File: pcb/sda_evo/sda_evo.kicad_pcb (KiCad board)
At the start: 4 copper layers, 61.5 x 105.9 mm, 156 parts, among them J1 PROG, J10 SPKR, J11 AudioJack, J2 USB_C_Receptacle_USB2.0, J3 LCD_CONN, J4 INT_EXP, J5 BATT, J9 Micro_SD_Card_Det, Q1 IRLML6302, SW1 RESET, SW2 BTN_A, SW3 BTN_B, SW4 BTN_UP, SW5 BTN_DOWN, SW6 BTN_LEFT, SW7 BTN_RIGHT, SW8 BTN_PWR, U1 USBLC6, U10 STM32H743ZITx, U11 USBLC6, U12 AP22802AW5-7, U13 LM4861, U2 TLV431, U3 USBLC6, U4 AP22802AW5-7, U5 FT230XS, U6 MCP73831-2-OT, U7 PCM5102, U8 NCP1529, U9 LMR62014XMF, Y1 16Mhz, Y2 32.768

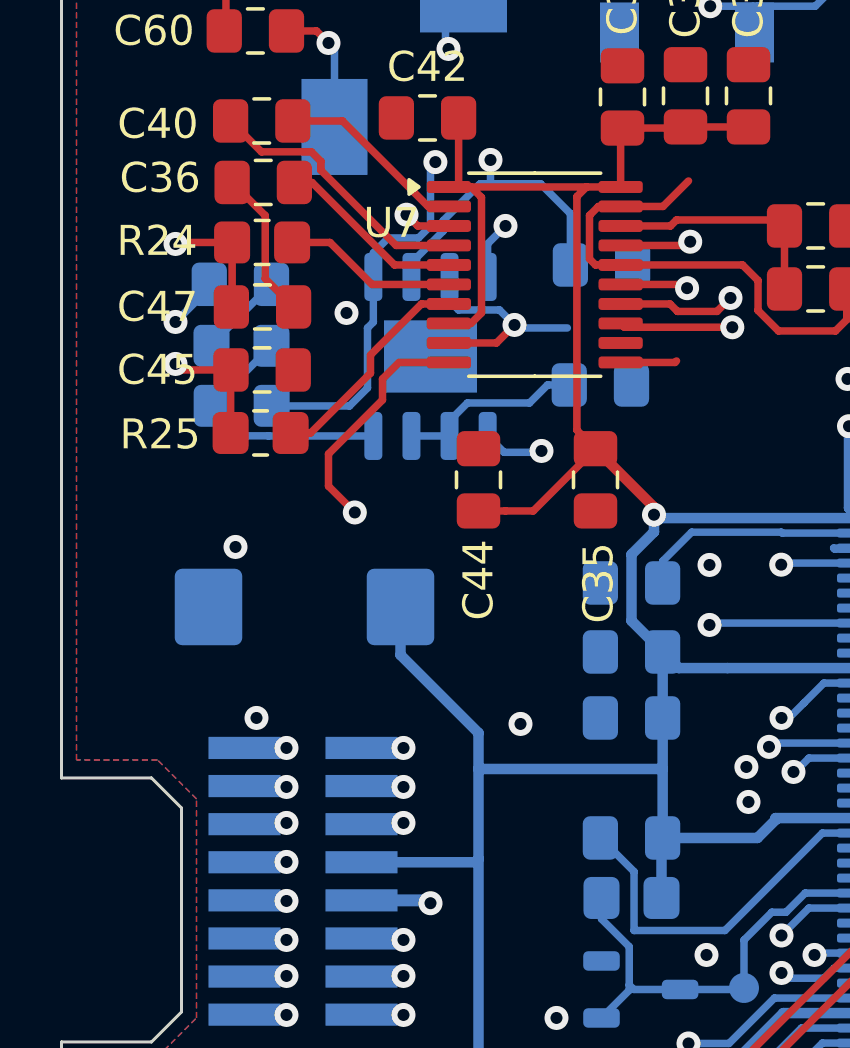
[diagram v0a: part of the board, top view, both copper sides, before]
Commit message: cap moved out of te way
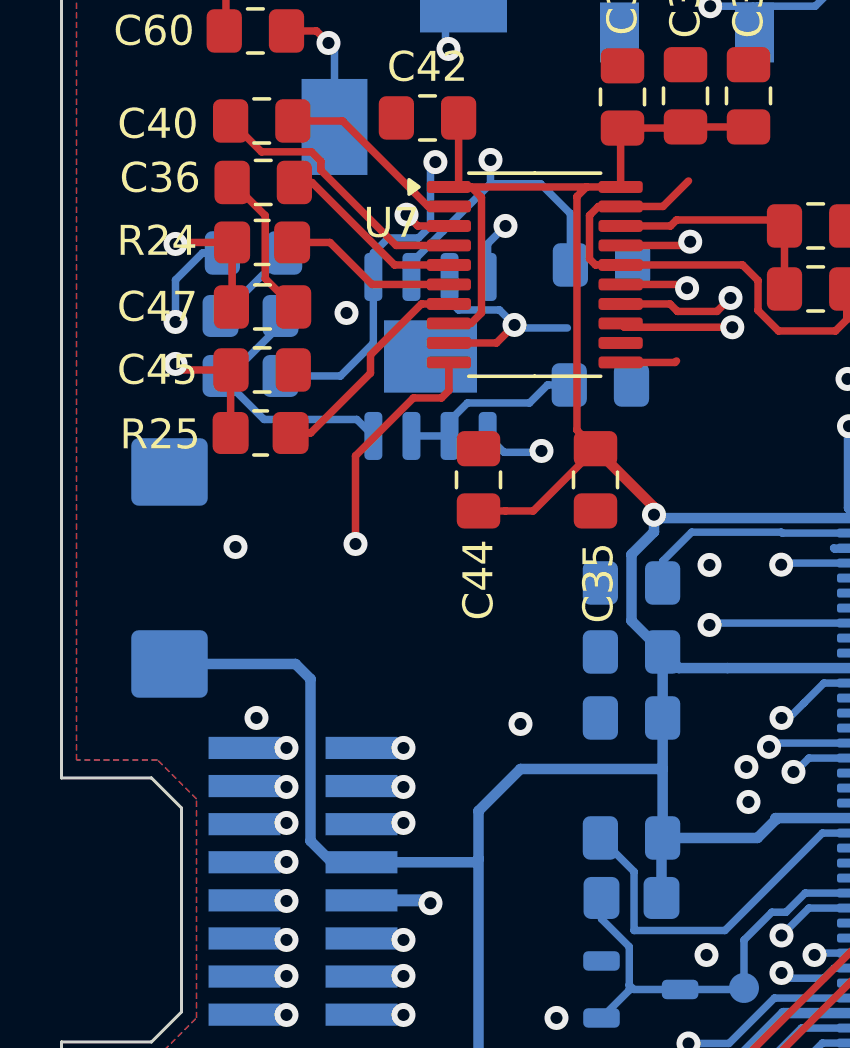
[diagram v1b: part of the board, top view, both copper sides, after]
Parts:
- moved C20 4.68 mm to (62.1, 80.0), turned to 90 degrees
- moved C58 1.13 mm to (64.9, 69.5)
- moved R35 1.04 mm to (64.8, 71.6)
- moved R31 1.04 mm to (64.8, 73.6)
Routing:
- net +3V3: track 478.2 -> 483.6 mm
- net BEEPER: track 39.2 -> 40.8 mm
- net Net-(C58-Pad2): track 2.99 -> 4.16 mm
- net Net-(J10-Pin_2): track 22.2 -> 21.3 mm

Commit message: datasheets cleanup, pcb finalized
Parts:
- added R30: 0, Resistor_SMD:R_0805_2012Metric_Pad1.20x1.40mm_HandSolder, B.Cu at (112.7, 86.4)
- added R37: 0, Resistor_SMD:R_0805_2012Metric_Pad1.20x1.40mm_HandSolder, B.Cu at (112.7, 88.4)
- added R38: 0, Resistor_SMD:R_0805_2012Metric_Pad1.20x1.40mm_HandSolder, F.Cu at (99.7, 109.0)
- added R39: 0, Resistor_SMD:R_0805_2012Metric_Pad1.20x1.40mm_HandSolder, F.Cu at (97.7, 109.0)
- added R40: 0, Resistor_SMD:R_0805_2012Metric_Pad1.20x1.40mm_HandSolder, F.Cu at (101.6, 109.0)
- moved TP7 6.35 mm to (113.0, 104.4)
- moved C7 1.25 mm to (112.7, 90.5)
- moved U4 0.65 mm to (100.5, 126.1)
- moved TP6 0.20 mm to (109.3, 104.4)
- moved C10 0.10 mm to (112.7, 84.4)
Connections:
- J3 pad 38: GND -> Net-(J3-Pin_38)
- J3 pad 39: +3V3 -> Net-(J3-Pin_39)
- J3 pad 40: GND -> Net-(J3-Pin_40)
- U10 pad 124: unconnected-(U10-PG9-Pad124) -> Net-(U10-PG9)
- U10 pad 125: unconnected-(U10-PG10-Pad125) -> Net-(U10-PG10)
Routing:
- net Net-(J3-Pin_39): track 0.00 -> 11.3 mm
- net Net-(U10-PG10): track 0.00 -> 6.14 mm
- net Net-(J3-Pin_40): track 0.00 -> 5.74 mm
- net Net-(U10-PG9): track 0.00 -> 5.52 mm
- net GND: track 244.7 -> 239.3 mm
- net Net-(J3-Pin_38): track 0.00 -> 5.24 mm
- net +3V3: track 483.6 -> 486.3 mm
- net VD: track 69.8 -> 68.4 mm
- net Net-(U12-OUT): track 12.2 -> 13.0 mm
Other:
- board text added: "Beta 0 XII. 2025 Designed in Budweis by Standa"
- board text removed: "Beta 0 V. 2025 Designed in Budweis by Standa"
